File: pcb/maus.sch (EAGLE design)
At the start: 90 parts, among them J1 SS-52300-001, Q1 BSS123, Q2 BSS123, Q3 BSS123, Q4 BSS123, Q5 BSS123, Q6 SI3499DV-T1-BE3, Q7 SI3499DV-T1-BE3, U1 ESP32-S2-WROOM, U2 CH340C, U3 CP2102, U4 LP3965EMP-3.3, U5 LSM9DS1TR, U6 LM358DR

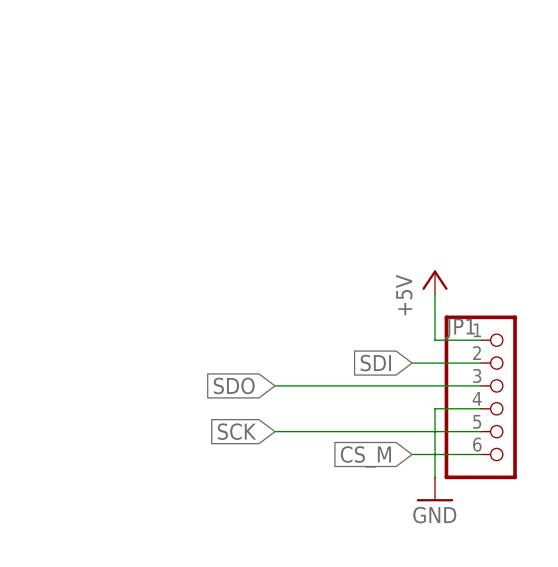
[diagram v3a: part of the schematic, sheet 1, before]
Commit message: fixup! added a SPI breakout
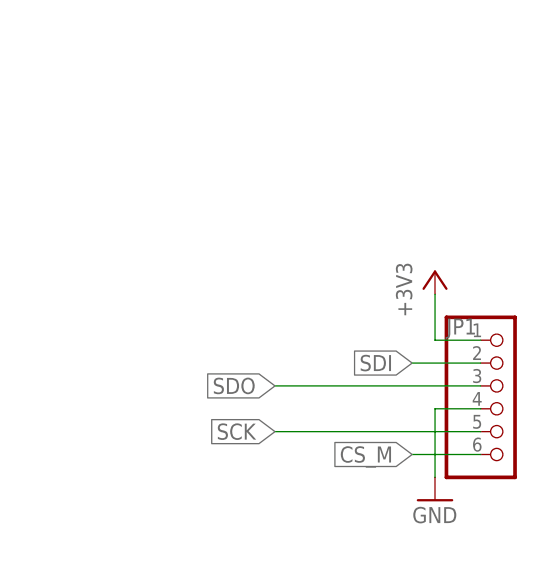
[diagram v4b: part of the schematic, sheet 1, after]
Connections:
- net +3V3: now also JP1.1
- net +5V: no longer JP1.1
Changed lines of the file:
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@@
 <part name="GND40" library="supply1" library_urn="urn:adsk.eagle:library:371" deviceset="GND" device=""/>
 <part name="JP1" library="pinhead" library_urn="urn:adsk.eagle:library:325" deviceset="PINHD-1X6" device="" package3d_urn="urn:adsk.eagle:package:22472/2"/>
-<part name="P+8" library="supply1" library_urn="urn:adsk.eagle:library:371" deviceset="+5V" device=""/>
 <part name="GND43" library="supply1" library_urn="urn:adsk.eagle:library:371" deviceset="GND" device=""/>
 <part name="J1" library="shared" deviceset="SS-52300-001" device=""/>
 <part name="R28" library="rcl" library_urn="urn:adsk.eagle:library:334" deviceset="R-EU_" device="R0805" package3d_urn="urn:adsk.eagle:package:23553/2" value="10k"/>
 <part name="+3V15" library="supply1" library_urn="urn:adsk.eagle:library:371" deviceset="+3V3" device=""/>
+<part name="+3V16" library="supply1" library_urn="urn:adsk.eagle:library:371" deviceset="+3V3" device=""/>
 </parts>
 <sheets>
@@
 <attribute name="VALUE" x="227.33" y="78.74" size="1.778" layer="96"/>
 </instance>
-<instance part="P+8" gate="1" x="226.06" y="104.14" smashed="yes">
-<attribute name="VALUE" x="223.52" y="99.06" size="1.778" layer="96" rot="R90"/>
-</instance>
 <instance part="GND43" gate="1" x="226.06" y="78.74" smashed="yes">
 <attribute name="VALUE" x="223.52" y="76.2" size="1.778" layer="96"/>
@@
 <instance part="+3V15" gate="G$1" x="182.88" y="38.1" smashed="yes">
 <attribute name="VALUE" x="180.34" y="33.02" size="1.778" layer="96" rot="R90"/>
+</instance>
+<instance part="+3V16" gate="G$1" x="226.06" y="104.14" smashed="yes">
+<attribute name="VALUE" x="223.52" y="99.06" size="1.778" layer="96" rot="R90"/>
 </instance>
 </instances>
@@
 <pinref part="R28" gate="G$1" pin="2"/>
 <wire x1="182.88" y1="35.56" x2="182.88" y2="33.02" width="0.1524" layer="91"/>
+</segment>
+<segment>
+<pinref part="JP1" gate="A" pin="1"/>
+<wire x1="231.14" y1="96.52" x2="226.06" y2="96.52" width="0.1524" layer="91"/>
+<wire x1="226.06" y1="96.52" x2="226.06" y2="101.6" width="0.1524" layer="91"/>
+<pinref part="+3V16" gate="G$1" pin="+3V3"/>
 </segment>
 </net>
@@
 </segment>
 </net>
-<net name="+5V" class="0">
-<segment>
-<pinref part="JP1" gate="A" pin="1"/>
-<pinref part="P+8" gate="1" pin="+5V"/>
-<wire x1="231.14" y1="96.52" x2="226.06" y2="96.52" width="0.1524" layer="91"/>
-<wire x1="226.06" y1="96.52" x2="226.06" y2="101.6" width="0.1524" layer="91"/>
-</segment>
-</net>

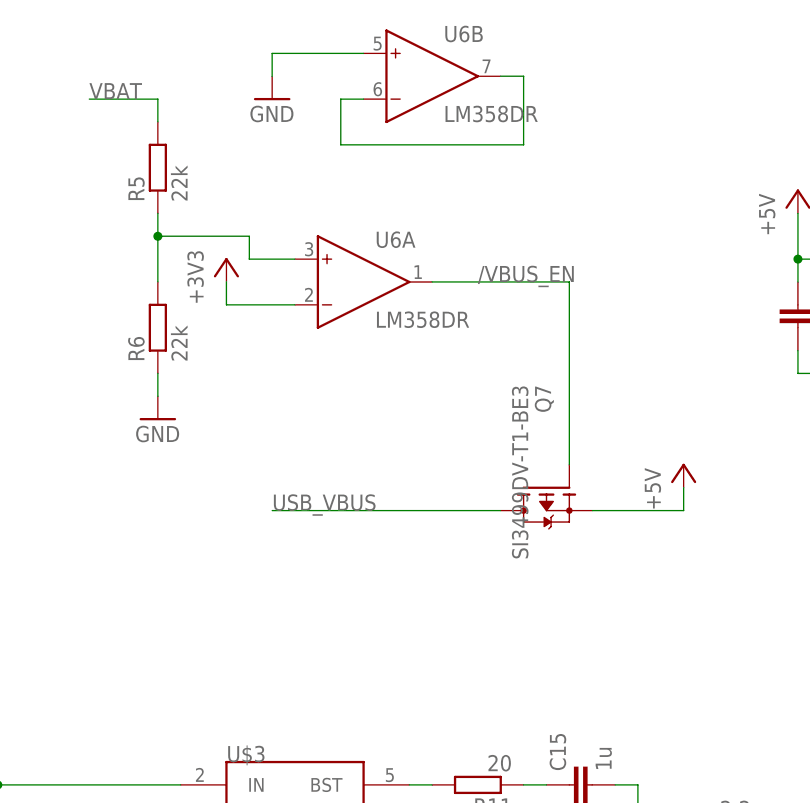
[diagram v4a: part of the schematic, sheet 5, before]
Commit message: now use new mosfet
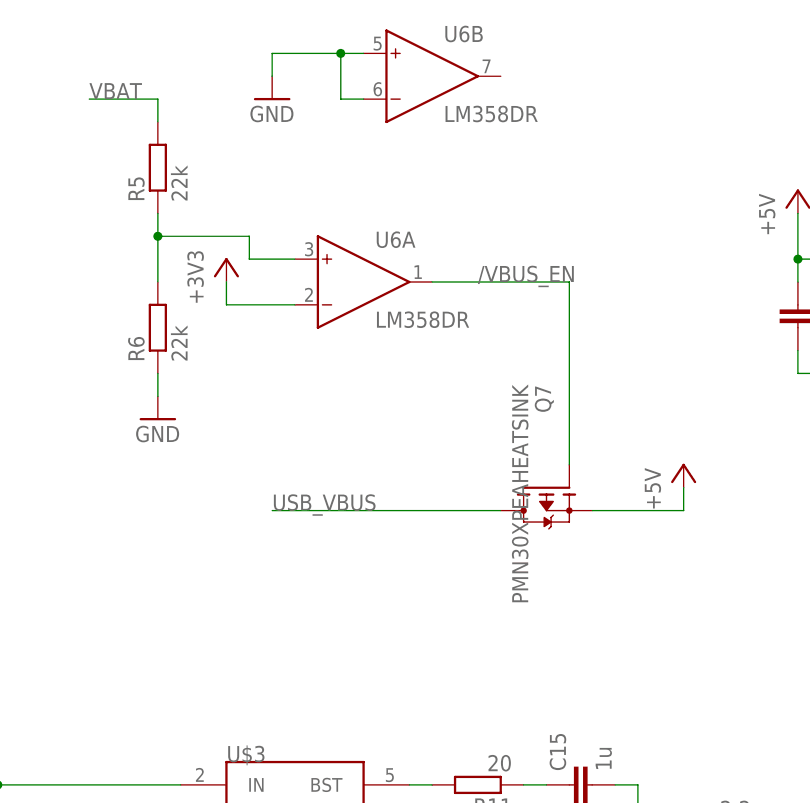
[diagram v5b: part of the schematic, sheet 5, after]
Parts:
- Q6, Q7: value SI3499DV-T1-BE3 -> PMN30XPEAHEATSINK; device mosfet:SI3499DV-T1-BE3 -> mosfet:PMN30XPEAHEATSINK
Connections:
- removed net N$9: U6B.IN-, U6B.OUT
- net GND: now also U6B.IN-
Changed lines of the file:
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@@
 <part name="R25" library="rcl" library_urn="urn:adsk.eagle:library:334" deviceset="R-EU_" device="R0805" package3d_urn="urn:adsk.eagle:package:23553/2" value="22k"/>
 <part name="GND41" library="supply1" library_urn="urn:adsk.eagle:library:371" deviceset="GND" device=""/>
-<part name="Q6" library="mosfet" deviceset="SI3499DV-T1-BE3" device="" package3d_urn="urn:adsk.eagle:package:33743404/1"/>
-<part name="Q7" library="mosfet" deviceset="SI3499DV-T1-BE3" device="" package3d_urn="urn:adsk.eagle:package:33743404/1"/>
+<part name="Q6" library="mosfet" deviceset="PMN30XPEA" device="HEATSINK" package3d_urn="urn:adsk.eagle:package:33743404/1"/>
+<part name="Q7" library="mosfet" deviceset="PMN30XPEA" device="HEATSINK" package3d_urn="urn:adsk.eagle:package:33743404/1"/>
 <part name="U6" library="LM358DR" deviceset="LM358DR" device="" package3d_urn="urn:adsk.eagle:package:33744331/1"/>
 <part name="GND42" library="supply1" library_urn="urn:adsk.eagle:library:371" deviceset="GND" device=""/>
@@
 </sheet>
 <sheet>
+<description>UART/Prog</description>
 <plain>
 <text x="40.64" y="7.62" size="1.778" layer="115">Auto program table
@@
 </sheet>
 <sheet>
+<description>IR</description>
 <plain>
 </plain>
@@
 </sheet>
 <sheet>
-<description>description</description>
+<description>power</description>
 <plain>
 <text x="251.46" y="50.8" size="1.778" layer="97">es soll die 3v3-Leitung an gehen, wenn das Gerät über USB
@@
 <pinref part="U6" gate="B" pin="IN+"/>
 <wire x1="66.04" y1="142.24" x2="66.04" y2="144.78" width="0.1524" layer="91"/>
-<wire x1="66.04" y1="144.78" x2="76.2" y2="144.78" width="0.1524" layer="91"/>
+<wire x1="66.04" y1="144.78" x2="73.66" y2="144.78" width="0.1524" layer="91"/>
+<pinref part="U6" gate="B" pin="IN-"/>
+<wire x1="73.66" y1="144.78" x2="76.2" y2="144.78" width="0.1524" layer="91"/>
+<wire x1="76.2" y1="139.7" x2="73.66" y2="139.7" width="0.1524" layer="91"/>
+<wire x1="73.66" y1="139.7" x2="73.66" y2="144.78" width="0.1524" layer="91"/>
+<junction x="73.66" y="144.78"/>
 </segment>
 </net>
@@
 </segment>
 </net>
-<net name="N$9" class="0">
-<segment>
-<pinref part="U6" gate="B" pin="IN-"/>
-<wire x1="76.2" y1="139.7" x2="73.66" y2="139.7" width="0.1524" layer="91"/>
-<wire x1="73.66" y1="139.7" x2="73.66" y2="134.62" width="0.1524" layer="91"/>
-<wire x1="73.66" y1="134.62" x2="93.98" y2="134.62" width="0.1524" layer="91"/>
-<wire x1="93.98" y1="134.62" x2="93.98" y2="142.24" width="0.1524" layer="91"/>
-<pinref part="U6" gate="B" pin="OUT"/>
-<wire x1="93.98" y1="142.24" x2="91.44" y2="142.24" width="0.1524" layer="91"/>
-</segment>
-</net>

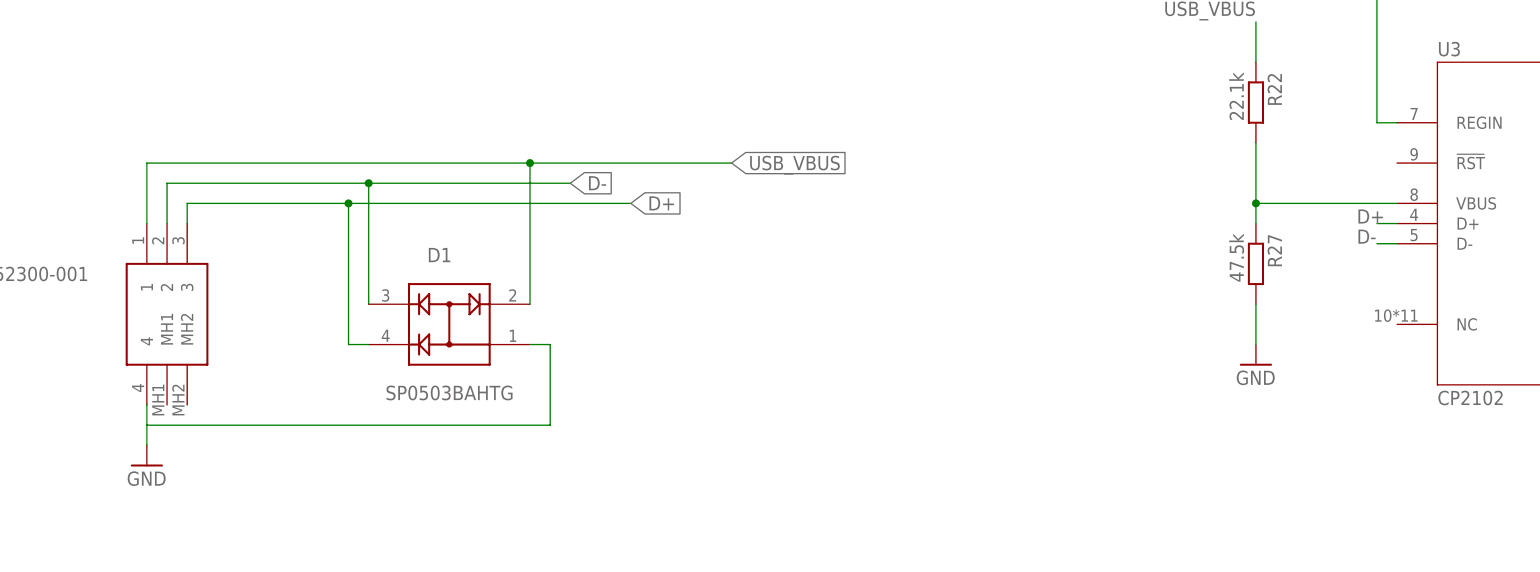
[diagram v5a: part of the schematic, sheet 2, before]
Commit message: fixed some ERC errors
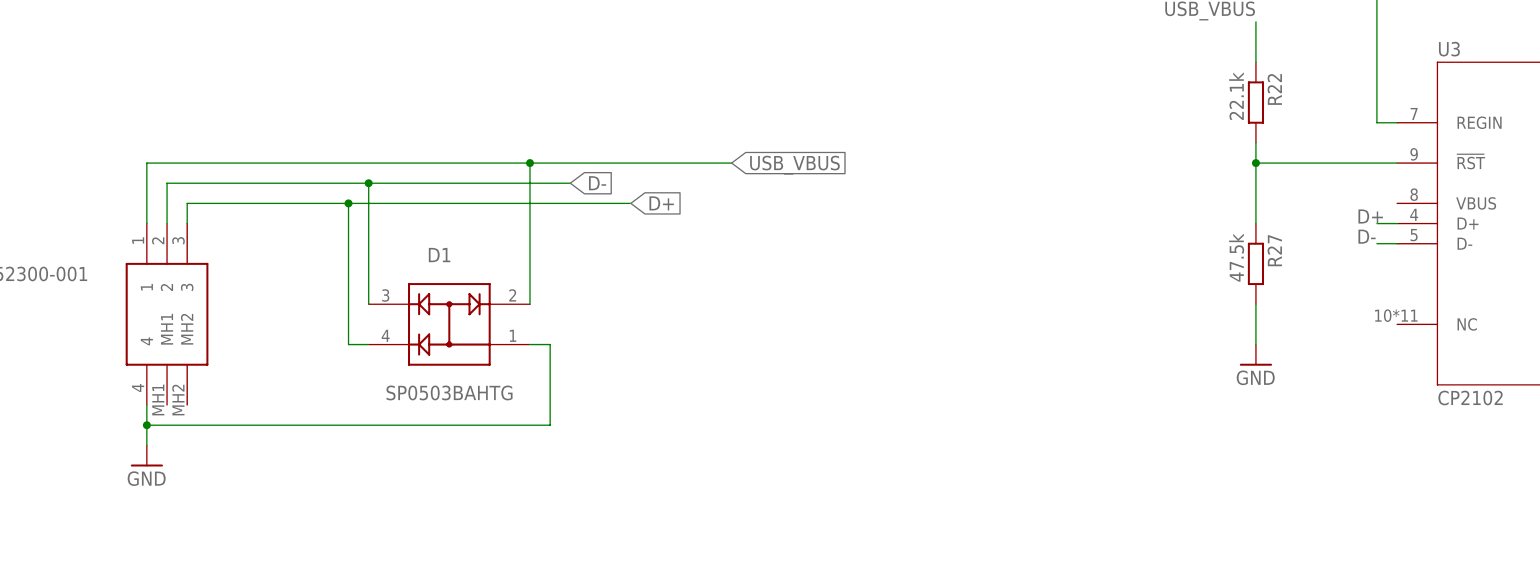
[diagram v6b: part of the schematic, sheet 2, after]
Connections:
- net GND: now also D1.1, J1.4
- net N$4: now also R22.2, R27.1, U3.!RST; no longer D1.1, J1.4
- net USB_VBUS: no longer R22.2, R27.1, U3.VBUS
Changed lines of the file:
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@@
-</segment>
-<segment>
-<pinref part="U3" gate="G$1" pin="VBUS"/>
-<wire x1="162.56" y1="129.54" x2="144.78" y2="129.54" width="0.1524" layer="91"/>
-<wire x1="144.78" y1="129.54" x2="144.78" y2="137.16" width="0.1524" layer="91"/>
-<pinref part="R22" gate="G$1" pin="2"/>
-<pinref part="R27" gate="G$1" pin="1"/>
-<wire x1="144.78" y1="127" x2="144.78" y2="129.54" width="0.1524" layer="91"/>
-<junction x="144.78" y="129.54"/>
 </segment>
 <segment>
@@
 <wire x1="205.74" y1="147.32" x2="205.74" y2="149.86" width="0.1524" layer="91"/>
 <junction x="205.74" y="149.86"/>
+</segment>
+<segment>
+<pinref part="J1" gate="G$1" pin="4"/>
+<wire x1="5.08" y1="104.14" x2="5.08" y2="101.6" width="0.1524" layer="91"/>
+<wire x1="5.08" y1="101.6" x2="55.88" y2="101.6" width="0.1524" layer="91"/>
+<pinref part="D1" gate="G$1" pin="1"/>
+<wire x1="53.34" y1="111.76" x2="55.88" y2="111.76" width="0.1524" layer="91"/>
+<wire x1="55.88" y1="111.76" x2="55.88" y2="101.6" width="0.1524" layer="91"/>
+<pinref part="GND29" gate="1" pin="GND"/>
+<wire x1="5.08" y1="99.06" x2="5.08" y2="101.6" width="0.1524" layer="91"/>
+<junction x="5.08" y="101.6"/>
 </segment>
 </net>
@@
 <net name="N$4" class="0">
 <segment>
-<pinref part="J1" gate="G$1" pin="4"/>
-<wire x1="5.08" y1="104.14" x2="5.08" y2="101.6" width="0.1524" layer="91"/>
-<wire x1="5.08" y1="101.6" x2="55.88" y2="101.6" width="0.1524" layer="91"/>
-<pinref part="D1" gate="G$1" pin="1"/>
-<wire x1="53.34" y1="111.76" x2="55.88" y2="111.76" width="0.1524" layer="91"/>
-<wire x1="55.88" y1="111.76" x2="55.88" y2="101.6" width="0.1524" layer="91"/>
-<wire x1="5.08" y1="99.06" x2="5.08" y2="101.6" width="0.1524" layer="91"/>
-<pinref part="GND29" gate="1" pin="GND"/>
-</segment>
-</net>
+<pinref part="R22" gate="G$1" pin="2"/>
+<pinref part="R27" gate="G$1" pin="1"/>
+<wire x1="144.78" y1="137.16" x2="144.78" y2="134.62" width="0.1524" layer="91"/>
+<pinref part="U3" gate="G$1" pin="!RST"/>
+<wire x1="144.78" y1="134.62" x2="144.78" y2="127" width="0.1524" layer="91"/>
+<wire x1="144.78" y1="134.62" x2="162.56" y2="134.62" width="0.1524" layer="91"/>
+<junction x="144.78" y="134.62"/>
+</segment>
+</net>

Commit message: maus board layout
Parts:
- removed C2: 100nF, rcl:C-EUC0805
- removed C5: 4.7uF, rcl:C-EUC0805
- removed R2: 10k, rcl:R-EU_R0805
- removed R22: 22.1k, rcl:R-EU_R0805
- removed R27: 47.5k, rcl:R-EU_R0805
- removed U3: CP2102, CP2102:CP2102
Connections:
- removed net N$3: R2.2, U3.!SUSPEND
- removed net N$4: R22.2, R27.1, U3.!RST
- net +3V3: no longer C2.1, C5.1, U3.REGIN, U3.VDD
- net D+: no longer U3.D+
- net D-: no longer U3.D-
- net DTR: no longer U3.DTR
- net ESP32_RX: no longer U3.TXD
- net ESP32_TX: no longer U3.RXD
- net GND: no longer C2.2, C5.2, R2.1, R27.2, U3.GND
- net RTS: no longer U3.RTS
- net USB_VBUS: no longer R22.1
